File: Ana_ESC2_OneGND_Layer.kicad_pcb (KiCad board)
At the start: 4 copper layers, 90 x 90 mm, 104 parts, among them IC1 TCAN330DCNT, J1 BM04B-GHS-TBT_LF__SN__N_, J2 USB_C_Receptacle_USB2.0_16P, J3 Conn_01x02_Socket, J4 Conn_01x04_Pin, J5 BM04B-GHS-TBT_LF__SN__N_, Q10 STL90N6F7, Q11 STL90N6F7, Q12 STL90N6F7, Q7 STL90N6F7, Q8 STL90N6F7, Q9 STL90N6F7, SW1 SW_SPDT, SW2 SW_SPDT, U1 DRV8323RSRGZR, U2 ME6211C33M5, U3 STM32G431CBU6, Y1 ECS-80-20-5PX-TR

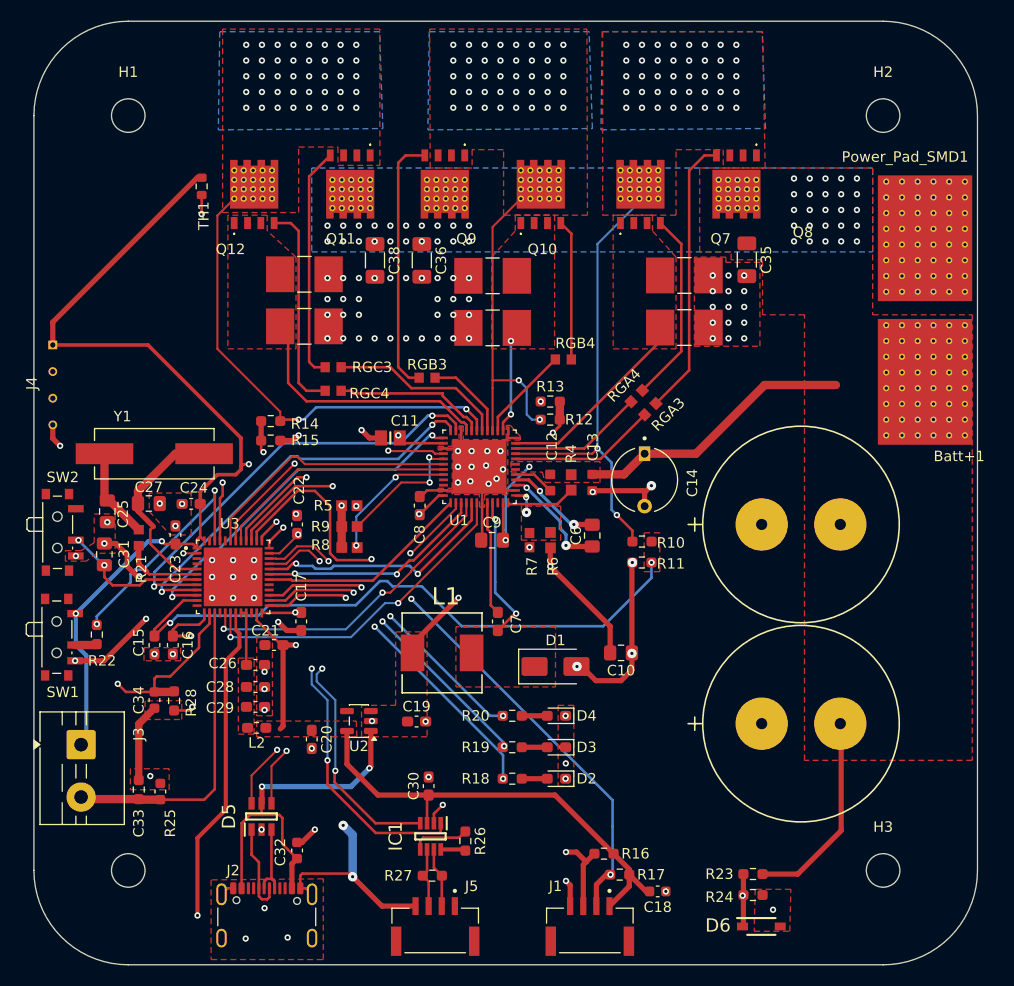
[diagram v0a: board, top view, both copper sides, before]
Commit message: BOM list prepared for ekom and direnc.net
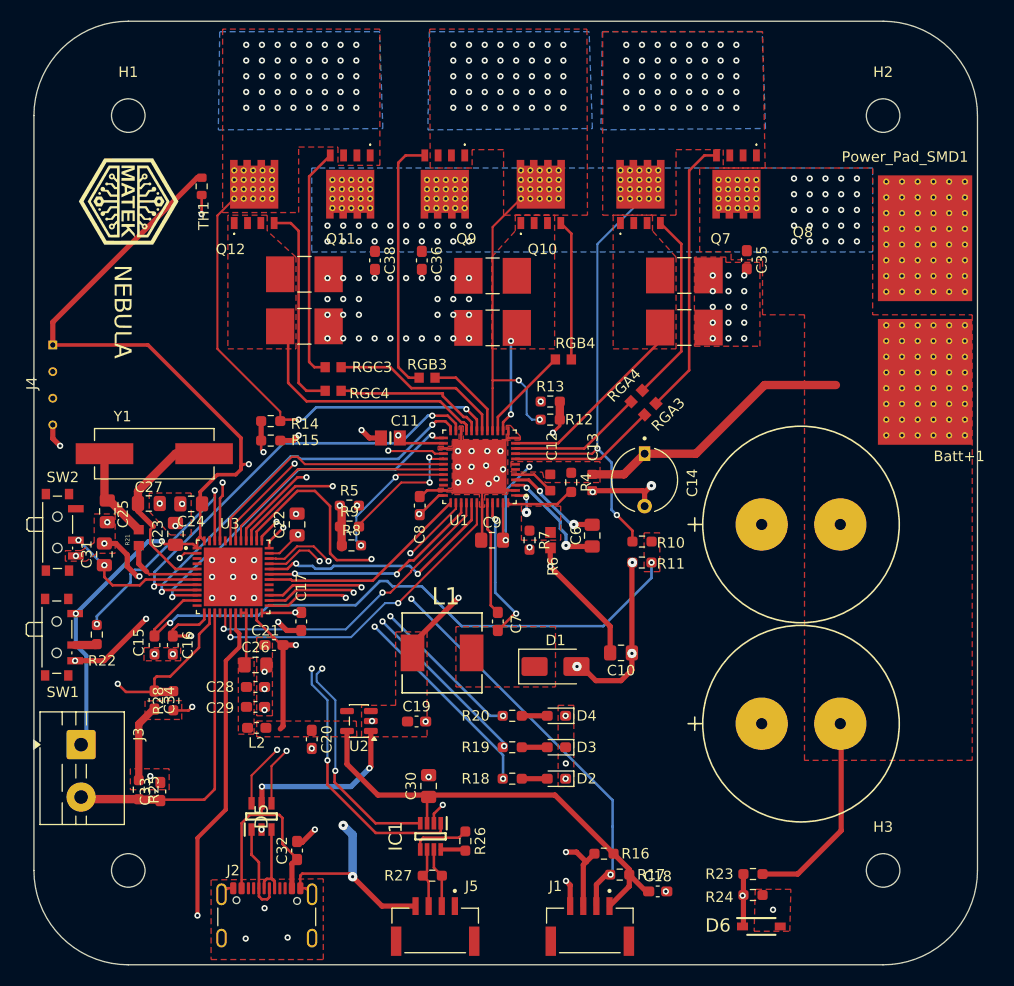
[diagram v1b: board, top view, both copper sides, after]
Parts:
- added G***: LOGO, LOGO, F.Cu at (57.5, 68.8)
- added G***: LOGO, LOGO, F.Cu at (57.1, 79.1)
- C18, C32, C33, C34: footprint Capacitor_SMD:C_0603_1608Metric -> Capacitor_SMD:C_0603_1608Metric_Pad1.08x0.95mm_HandSolder
- C19, C20: value 1u -> 1uF
- C22, C23, C24, C30: footprint Capacitor_SMD:C_0603_1608Metric_Pad1.08x0.95mm_HandSolder -> Capacitor_SMD:C_0805_2012Metric_Pad1.18x1.45mm_HandSolder
- C26: value 100n -> 100nF; footprint Capacitor_SMD:C_0603_1608Metric_Pad1.08x0.95mm_HandSolder -> Capacitor_SMD:C_0805_2012Metric_Pad1.18x1.45mm_HandSolder
- C35, C36, C38: footprint Capacitor_SMD:C_1206_3216Metric_Pad1.33x1.80mm_HandSolder -> Capacitor_SMD:C_0603_1608Metric_Pad1.08x0.95mm_HandSolder
- R21: value 0 ohm -> 0ohm
- R25, R28: value R_Small -> 1k
- R4: value 100K -> 100k; footprint RC0603FR-07100KL:RESC1607X60N -> Resistor_SMD:R_0603_1608Metric_Pad0.98x0.95mm_HandSolder
- R5, R8, R9: value 10K -> 10k; footprint RC0603FR-0710KL:RESC1607X60N -> Resistor_SMD:R_0603_1608Metric_Pad0.98x0.95mm_HandSolder
- R7: footprint RNCP0603FTD1K00:RESC1508X50N -> Resistor_SMD:R_0603_1608Metric_Pad0.98x0.95mm_HandSolder
- moved R8 0.27 mm to (78.8, 101.5), turned to 0 degrees
- moved C23 0.10 mm to (62.0, 100.4)
- moved R28 0.07 mm to (61.8, 116.3), turned to 90 degrees
- turned R25 to -90 degrees
- turned R21 to 90 degrees
- turned R5 to 0 degrees
- turned R9 to 0 degrees
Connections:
- R21 pad 1: Net-(C25-Pad1) -> Net-(U3-PF1-OSC_OUT)
- R21 pad 2: Net-(U3-PF1-OSC_OUT) -> Net-(C25-Pad1)
- R25 pad 1: /MCU/NTC_MTR -> GND2
- R25 pad 2: GND2 -> /MCU/NTC_MTR
- R28 pad 1: /MCU/NTC_FET -> GND2
- R28 pad 2: GND2 -> /MCU/NTC_FET
- R5 pad 1: /Gate_Driver/FAULT -> /Gate_Driver/DVDD
- R5 pad 2: /Gate_Driver/DVDD -> /Gate_Driver/FAULT
- R8 pad 1: Net-(U1-SCS_N) -> /Gate_Driver/DVDD
- R8 pad 2: /Gate_Driver/DVDD -> Net-(U1-SCS_N)
- R9 pad 1: /Gate_Driver/SDO -> /Gate_Driver/DVDD
- R9 pad 2: /Gate_Driver/DVDD -> /Gate_Driver/SDO
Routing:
- net /Gate_Driver/INLA: track 29.9 -> 31.1 mm
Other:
- board text added: "ABDEL MANAN ABDEL RAHMAN ALPEREN ŞAHİN 2026/05"

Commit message: for LCSC components the layout/footprints changed. Previous commit for ekom/direncnet components.
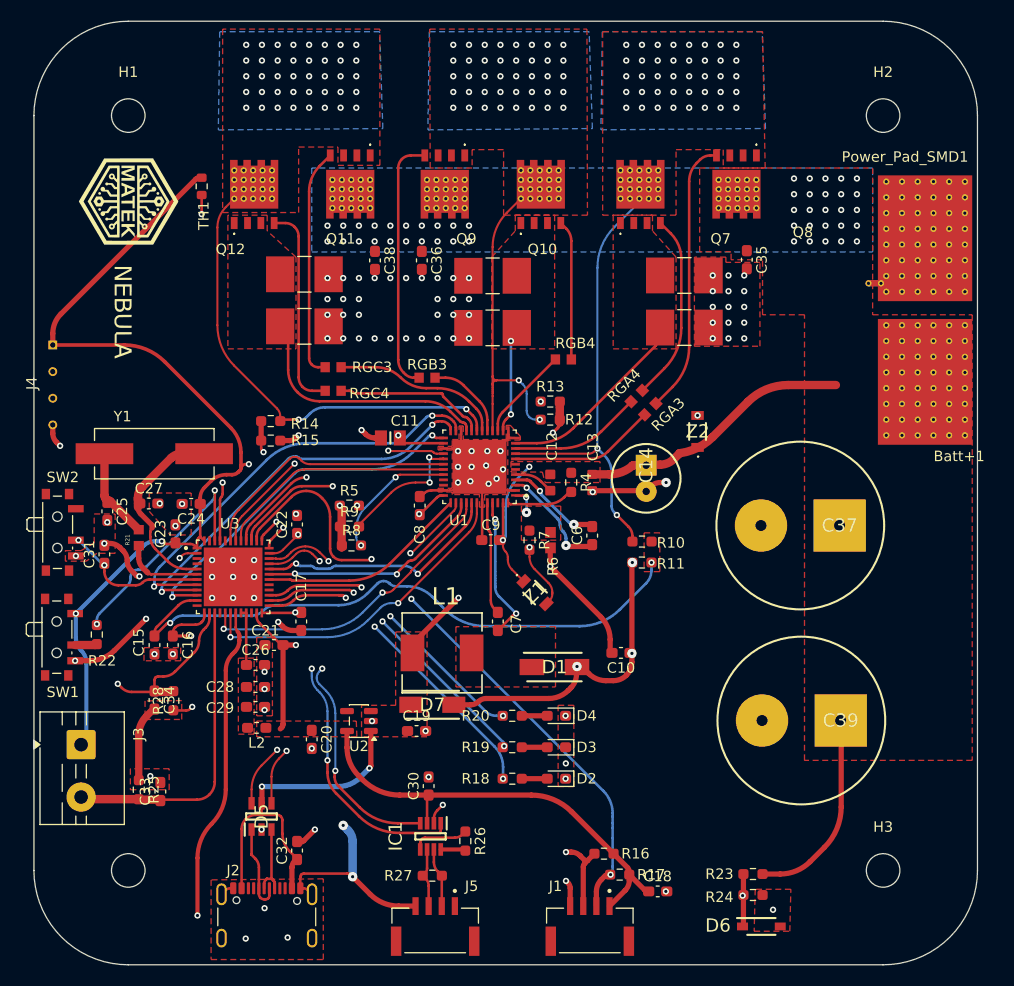
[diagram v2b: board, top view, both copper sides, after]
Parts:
- added D7: SMAJ5.0A-E3_61, LIB_SMAJ5.0A-E3_61:DIOM5127X229N, F.Cu at (86.5, 116.7)
- added NT1: NetTie_2, NetTie:NetTie-2_THT_Pad0.3mm, F.Cu at (129.3, 76.5)
- added Z1: KDZLVTR56, LIB_KDZLVTR56:KDZLVTR56, F.Cu at (96.3, 106.0)
- added Z2: KDZLVTR56, LIB_KDZLVTR56:KDZLVTR56, F.Cu at (111.8, 90.6)
- C10, C22, C23, C24, C25, C26, C27, C30, C31, C6, C9: footprint Capacitor_SMD:C_0805_2012Metric_Pad1.18x1.45mm_HandSolder -> Capacitor_SMD:C_0603_1608Metric_Pad1.08x0.95mm_HandSolder
- C14: footprint ECA2AM220B:CAPPRD500W50D630H1120 -> LIB_100YXJ22M6.3X11:CAPPRD250W50D655H1250
- C37, C39: footprint ul_80ZLJ680MGC18X25:80ZLJ680MGC18X25 -> LIB_EEUFS1K681:CAPPRD750W85D1600H2700
- D1: value 80V 1A -> SS18 80V 1A; footprint Diode_SMD:D_SMA -> LIB_SS18:DIOM5227X270N
- moved C39 7.54 mm to (125.5, 118.2), turned to 180 degrees
- moved C37 7.43 mm to (125.3, 99.6), turned to 180 degrees
- moved C14 1.41 mm to (106.9, 93.8)
- moved C19 0.91 mm to (85.0, 119.2)
- moved C9 0.12 mm to (92.1, 101.0)
- moved D1 0.11 mm to (98.2, 113.1)
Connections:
- C37 pad 1: GND -> VM
- C37 pad 2: VM -> GND
- C39 pad 1: GND -> VM
- C39 pad 2: VM -> GND
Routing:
- net (no net): track 0.00 -> 26.1 mm
- net GND: track 57.4 -> 80.1 mm, vias 68 -> 69
- net VM: track 57.7 -> 61.0 mm
- net /Gate_Driver/SENS1: track 60.6 -> 58.8 mm
- net GND2: track 64.6 -> 63.2 mm
- net /Gate_Driver/SENS2: track 57.9 -> 56.6 mm
- net /MCU/UART_N: track 51.1 -> 50.2 mm
- net MCU_PWR: track 64.8 -> 63.9 mm
- net /MCU/VBus: track 88.9 -> 88.0 mm
- net /MCU/I2C1_SCL: track 62.7 -> 61.8 mm
- net /MCU/UART_P: track 52.7 -> 51.9 mm
- net /Gate_Driver/SHC: track 45.2 -> 44.4 mm
- net /MCU/USB_DN: track 32.8 -> 32.1 mm
- net /MCU/USB_DP: track 33.0 -> 32.3 mm
- net /Gate_Driver/SOB: track 39.2 -> 38.5 mm
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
